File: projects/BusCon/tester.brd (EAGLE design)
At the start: 125.7 x 132.1 mm, 30 parts, among them IC1 74LS93N, IC10 74LS07N, IC11 74LS07N, IC12 74LS07N, IC13 74LS07N, IC14 74LS07N, IC15 74LS682N, IC16 74LS682N, IC17 74LS682N, IC18 74LS682N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

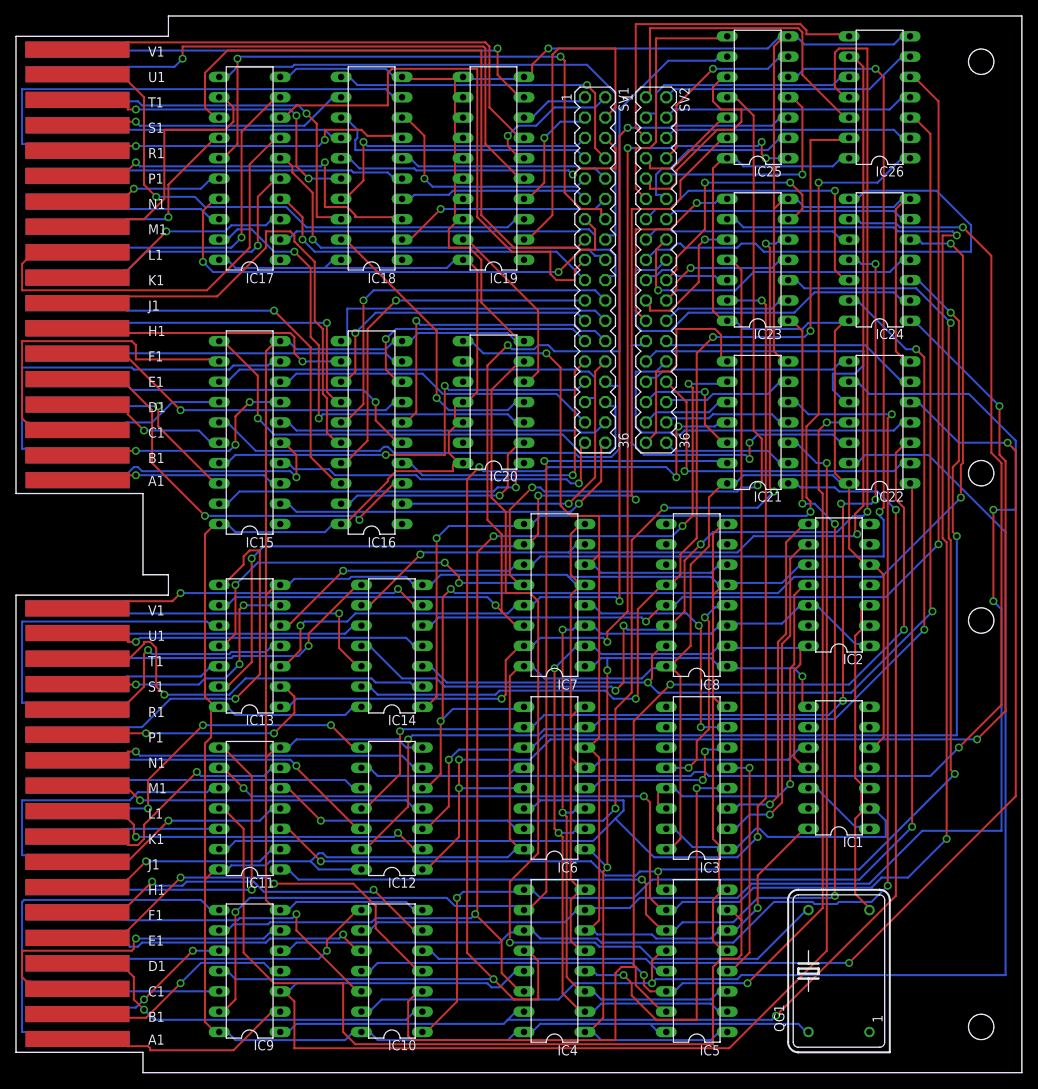
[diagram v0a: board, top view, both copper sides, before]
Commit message: Where possible, map 74xx-jameco to 74xx-us. Moved the 7438 to dec-con.lbr. Also changed the spelling of CRYTAL to CRYSTAL.
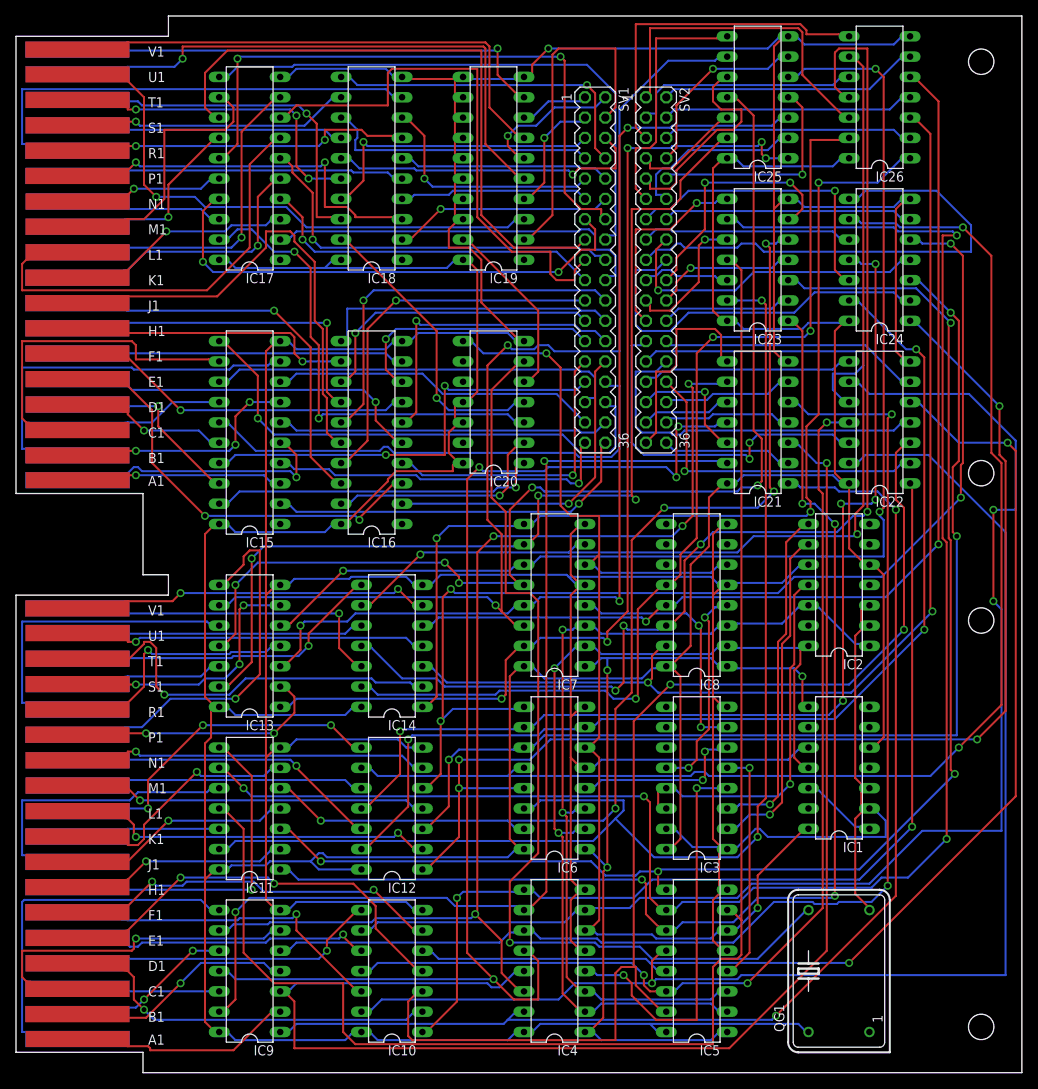
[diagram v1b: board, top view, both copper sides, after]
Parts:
- IC15, IC16, IC17, IC18, IC19: device 74xx-eu:DIL20 -> 74xx-us:DIL20
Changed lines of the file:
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@@
 <layer number="95" name="Names" color="7" fill="1" visible="no" active="no"/>
 <layer number="96" name="Values" color="7" fill="1" visible="no" active="no"/>
+<layer number="97" name="Info" color="7" fill="1" visible="no" active="no"/>
+<layer number="98" name="Guide" color="6" fill="1" visible="no" active="no"/>
 <layer number="250" name="Descript" color="3" fill="1" visible="no" active="no"/>
 <layer number="251" name="SMDround" color="12" fill="11" visible="no" active="no"/>
@@
 <element name="IC8" library="74xx-us" package="DIL16" value="74LS138N" x="85.09" y="59.69" rot="R90"/>
 <element name="IC20" library="74xx-us" package="DIL14" value="74LS30N" x="59.69" y="83.82" rot="R90"/>
-<element name="IC15" library="74xx-eu" package="DIL20" value="74LS682N" x="29.21" y="80.01" rot="R90"/>
+<element name="IC15" library="74xx-us" package="DIL20" value="74LS682N" x="29.21" y="80.01" rot="R90"/>
 <element name="IC9" library="74xx-us" package="DIL14" value="74LS07N" x="29.21" y="12.7" rot="R90"/>
 <element name="IC10" library="74xx-us" package="DIL14" value="74LS07N" x="46.99" y="12.7" rot="R90"/>
@@
 <element name="IC13" library="74xx-us" package="DIL14" value="74LS07N" x="29.21" y="53.34" rot="R90"/>
 <element name="IC14" library="74xx-us" package="DIL14" value="74LS07N" x="46.99" y="53.34" rot="R90"/>
-<element name="IC16" library="74xx-eu" package="DIL20" value="74LS682N" x="44.45" y="80.01" rot="R90"/>
-<element name="IC17" library="74xx-eu" package="DIL20" value="74LS682N" x="29.21" y="113.03" rot="R90"/>
-<element name="IC18" library="74xx-eu" package="DIL20" value="74LS682N" x="44.45" y="113.03" rot="R90"/>
-<element name="IC19" library="74xx-eu" package="DIL20" value="74LS682N" x="59.69" y="113.03" rot="R90"/>
+<element name="IC16" library="74xx-us" package="DIL20" value="74LS682N" x="44.45" y="80.01" rot="R90"/>
+<element name="IC17" library="74xx-us" package="DIL20" value="74LS682N" x="29.21" y="113.03" rot="R90"/>
+<element name="IC18" library="74xx-us" package="DIL20" value="74LS682N" x="44.45" y="113.03" rot="R90"/>
+<element name="IC19" library="74xx-us" package="DIL20" value="74LS682N" x="59.69" y="113.03" rot="R90"/>
 <element name="SV1" library="con-lstb" package="MA18-2" value="" x="72.39" y="100.33" rot="R270"/>
 <element name="SV2" library="con-lstb" package="MA18-2" value="" x="80.01" y="100.33" rot="R270"/>

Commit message: Walk the project tree, making things pass current design rules.
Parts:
- added U$2: OUTLINE-DOUBLE, dec-con:DOUBLE
- U$1: device dec-con:DOUBLE -> dec-con:EDGE-CON4
- moved IC20 76.2 mm to (73.7, 8.89), turned to 180 degrees
- moved IC2 71.9 mm to (53.3, 8.89), turned to 180 degrees
- moved QG1 68.6 mm to (49.5, 55.9)
- moved IC22 37.4 mm to (71.1, 74.9), turned to 180 degrees
- moved IC26 37.0 mm to (71.1, 125.7), turned to 180 degrees
- moved IC24 36.9 mm to (71.1, 100.3), turned to 180 degrees
- moved IC3 35.9 mm to (49.5, 31.8), turned to 270 degrees
- moved IC6 34.1 mm to (97.8, 21.6), turned to 180 degrees
- moved IC1 33.6 mm to (73.7, 21.6), turned to 180 degrees
- moved IC7 33.0 mm to (97.8, 47.0), turned to 180 degrees
- moved IC21 30.5 mm to (71.1, 59.7), turned to 180 degrees
- moved IC19 28.4 mm to (34.3, 125.7), turned to 180 degrees
- moved IC8 28.4 mm to (97.8, 34.3), turned to 180 degrees
- moved IC12 27.9 mm to (71.1, 47.0), turned to 180 degrees
- moved IC23 25.7 mm to (71.1, 87.6), turned to 180 degrees
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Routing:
- net OK2: track 28.2 -> 252.5 mm, vias 1 -> 4
- net OK4: track 36.9 -> 250.6 mm, vias 1 -> 2
- net OK5: track 22.8 -> 231.1 mm, vias 0 -> 3
- net GND: track 664.6 -> 506.8 mm
- net U1: track 138.1 -> 284.5 mm
- net OK3: track 59.3 -> 200.1 mm, vias 2 -> 6
- net V1: track 129.0 -> 250.8 mm
- net U2: track 151.6 -> 265.9 mm, vias 4 -> 3
- net AN2: track 39.1 -> 148.4 mm, vias 1 -> 5
- net VCC: track 534.1 -> 435.5 mm, vias 0 -> 6
- net AL1: track 45.8 -> 142.2 mm, vias 2 -> 7
- net K1: track 135.5 -> 220.8 mm, vias 5 -> 4
- net T1: track 124.6 -> 203.7 mm, vias 3 -> 4
- net F1: track 144.6 -> 222.1 mm, vias 2 -> 3
- net H1: track 151.7 -> 223.5 mm, vias 4 -> 5
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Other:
- outline, holes or cut-outs redrawn
